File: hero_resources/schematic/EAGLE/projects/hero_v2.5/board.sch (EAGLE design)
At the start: 43 parts, among them IC1 TP4056, IC2 4051D

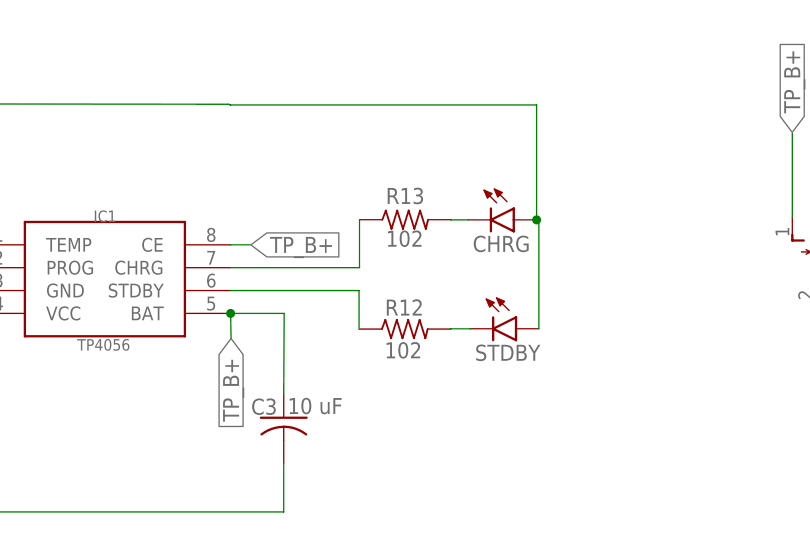
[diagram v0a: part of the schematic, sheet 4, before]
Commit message: Fix board v2.5 charge power led to 0805.
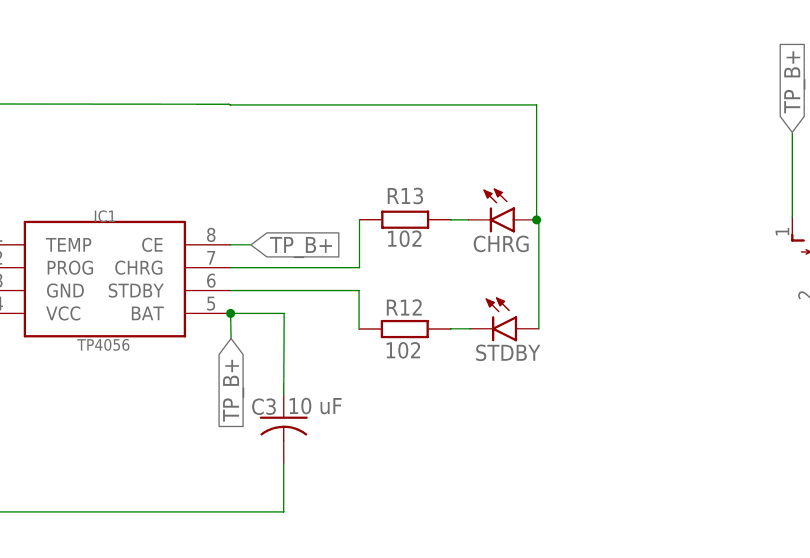
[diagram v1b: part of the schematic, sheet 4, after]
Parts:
- CHRG, STDBY: device led:LEDCHIP-LED0603 -> led:LEDSML0805
- R12, R13: device resistor:R-US_R0603 -> resistor:R-EU_R0805

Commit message: Update eagle projects; BOM available
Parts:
- R12: value 102 -> 103
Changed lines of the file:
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@@
 <?xml version="1.0" encoding="utf-8"?>
 <!DOCTYPE eagle SYSTEM "eagle.dtd">
-<eagle version="9.2.2">
+<eagle version="9.5.2">
 <drawing>
 <settings>
@@
 <attribute name="SPICEPREFIX" value="X"/>
 </part>
-<part name="R12" library="resistor" library_urn="urn:adsk.eagle:library:348" deviceset="R-EU_" device="R0805" package3d_urn="urn:adsk.eagle:package:23553/2" value="102"/>
+<part name="R12" library="resistor" library_urn="urn:adsk.eagle:library:348" deviceset="R-EU_" device="R0805" package3d_urn="urn:adsk.eagle:package:23553/2" value="103"/>
 <part name="R13" library="resistor" library_urn="urn:adsk.eagle:library:348" deviceset="R-EU_" device="R0805" package3d_urn="urn:adsk.eagle:package:23553/2" value="102"/>
 <part name="P+6" library="supply1" library_urn="urn:adsk.eagle:library:371" deviceset="VCC" device=""/>
